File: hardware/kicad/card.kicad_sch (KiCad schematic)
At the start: 13 parts, among them J3 Bus_Apple_II_Card_Side, U11 SN74LVC8T245, U12 SN74LVC8T245, U13 SN74LVC8T245, U14 SN74LVC8T245, U8 SN74LVC8T245, U9 SN74LVC8T245

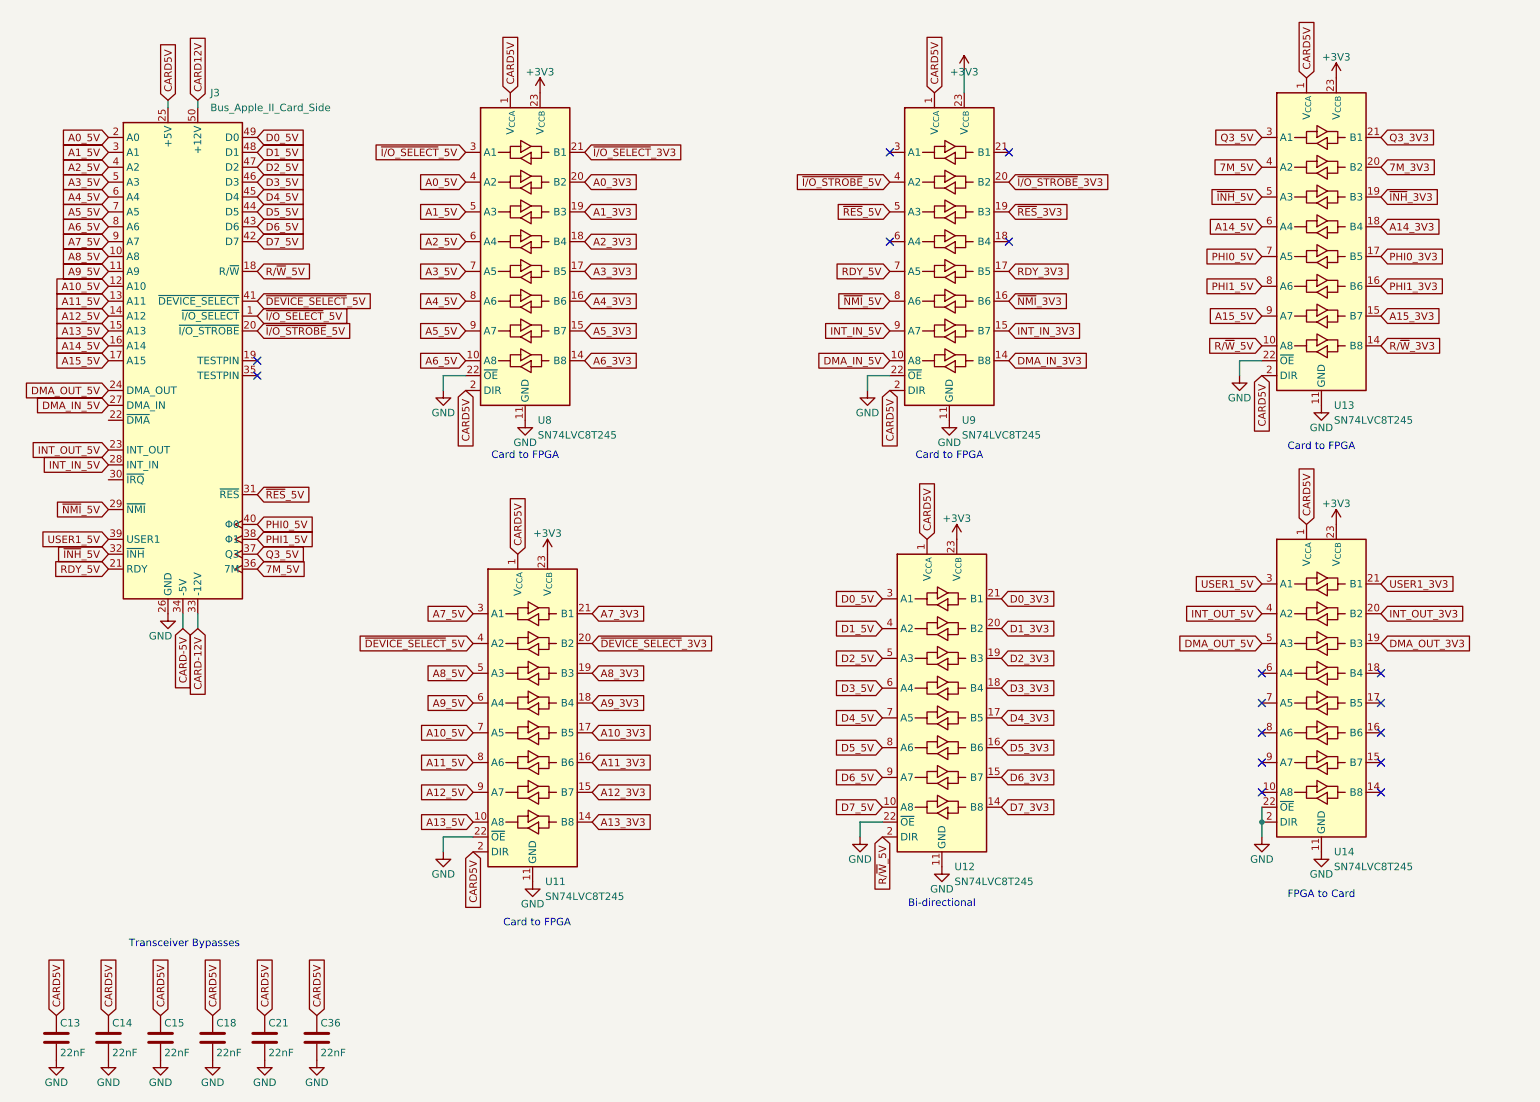
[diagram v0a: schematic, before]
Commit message: Updated Rev. 1.1
- Wired Level Shifters
- Expansion GPIOs
- Oscillator
- Flash
- USB
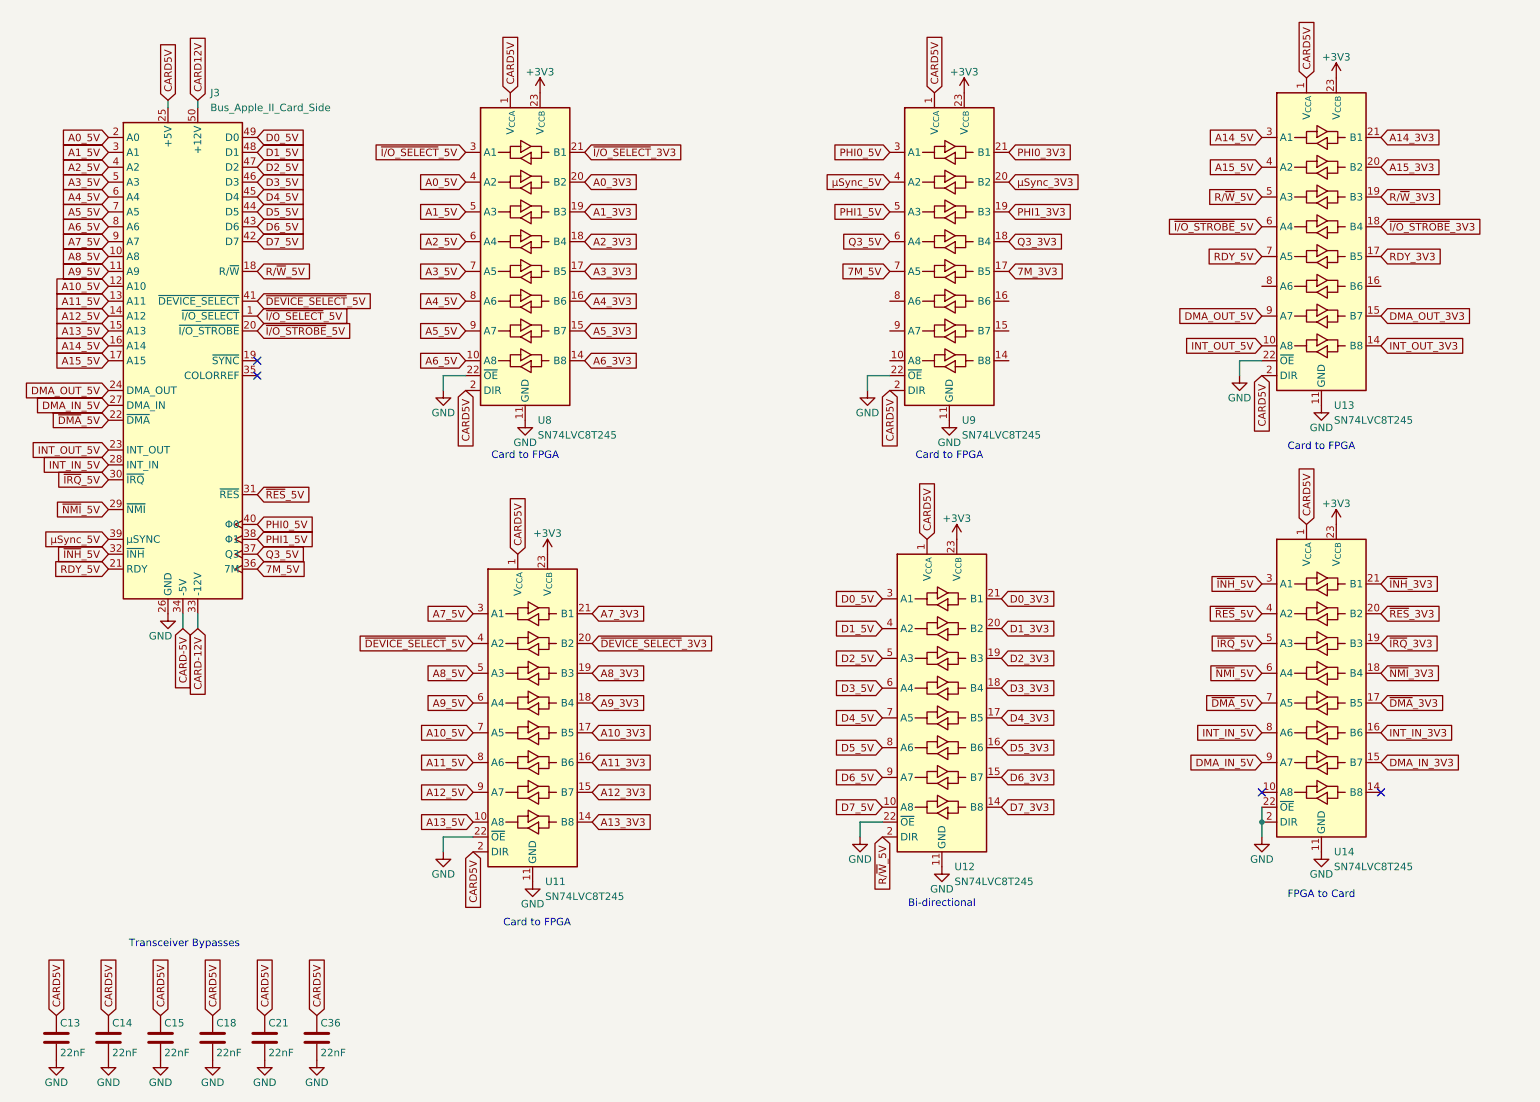
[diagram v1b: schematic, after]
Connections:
- net USER1_3V3 is gone; now on net ~{INH}_3V3: U14.21 (B1)
- net 7M_3V3: now also U9.17 (B5); no longer U13.20 (B2)
- net 7M_5V: now also U9.7 (A5); no longer U13.4 (A2)
- net A14_3V3: now also U13.21 (B1); no longer U13.18 (B4)
- net A14_5V: now also U13.3 (A1); no longer U13.6 (A4)
- net A15_3V3: now also U13.20 (B2); no longer U13.15 (B7)
- net A15_5V: now also U13.4 (A2); no longer U13.9 (A7)
- net DMA_IN_3V3: now also U14.15 (B7); no longer U9.14 (B8)
- net DMA_IN_5V: now also U14.9 (A7); no longer U9.10 (A8)
- net DMA_OUT_3V3: now also U13.15 (B7); no longer U14.19 (B3)
- net DMA_OUT_5V: now also U13.9 (A7); no longer U14.5 (A3)
- net INT_IN_3V3: now also U14.16 (B6); no longer U9.15 (B7)
- net INT_IN_5V: now also U14.8 (A6); no longer U9.9 (A7)
- net INT_OUT_3V3: now also U13.14 (B8); no longer U14.20 (B2)
- net INT_OUT_5V: now also U13.10 (A8); no longer U14.4 (A2)
- net PHI0_3V3: now also U9.21 (B1); no longer U13.17 (B5)
- net PHI0_5V: now also U9.3 (A1); no longer U13.7 (A5)
- net PHI1_3V3: now also U9.19 (B3); no longer U13.16 (B6)
- net PHI1_5V: now also U9.5 (A3); no longer U13.8 (A6)
- net Q3_3V3: now also U9.18 (B4); no longer U13.21 (B1)
- net Q3_5V: now also U9.6 (A4); no longer U13.3 (A1)
- net RDY_3V3: now also U13.17 (B5); no longer U9.17 (B5)
- net RDY_5V: now also U13.7 (A5); no longer U9.7 (A5)
- net R/~{W}_3V3: now also U13.19 (B3); no longer U13.14 (B8)
- net R/~{W}_5V: now also U13.5 (A3); no longer U13.10 (A8)
- net ~{INH}_3V3: no longer U13.19 (B3)
- net ~{INH}_5V: now also U14.3 (A1); no longer U13.5 (A3)
- net ~{I/O_STROBE}_3V3: now also U13.18 (B4); no longer U9.20 (B2)
- net ~{I/O_STROBE}_5V: now also U13.6 (A4); no longer U9.4 (A2)
- net ~{NMI}_3V3: now also U14.18 (B4); no longer U9.16 (B6)
- net ~{NMI}_5V: now also U14.6 (A4); no longer U9.8 (A6)
- net ~{RES}_3V3: now also U14.20 (B2); no longer U9.19 (B3)
- net ~{RES}_5V: now also U14.4 (A2); no longer U9.5 (A3)
- net ~{DMA}_5V: now reaches J3.22 (~{DMA})
- net ~{DMA}_5V: now also U14.7 (A5)
- net ~{IRQ}_5V: now reaches J3.30 (~{IRQ})
- net ~{IRQ}_5V: now also U14.5 (A3)
- net ~{DMA}_3V3: now reaches U14.17 (B5)
- net USER1_5V renamed µSync_5V
- net µSync_5V: now also U9.4 (A2); no longer U14.3 (A1)
- new net ~{IRQ}_3V3: U14.19 (B3)
- new net µSync_3V3: U9.20 (B2)
- no-connect marks 16 -> 4
